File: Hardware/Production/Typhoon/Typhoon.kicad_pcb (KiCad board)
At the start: 4 copper layers, 16 parts, among them U3 LM66200DRLR, U4 MAX77827AEFD+T, U5 SC4215ASTRT

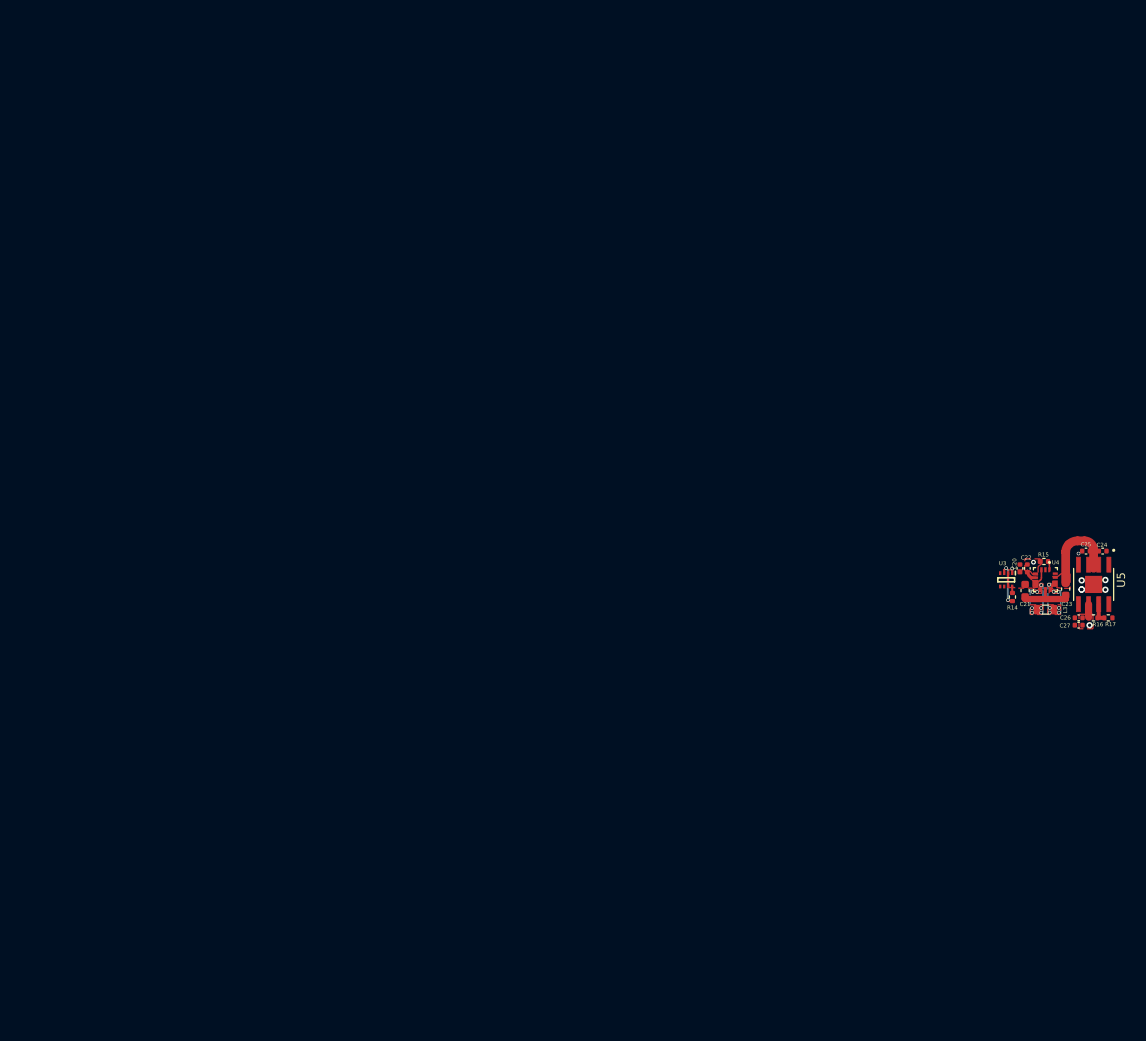
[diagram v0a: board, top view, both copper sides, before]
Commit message: Finished footprinting and started the PCB layout
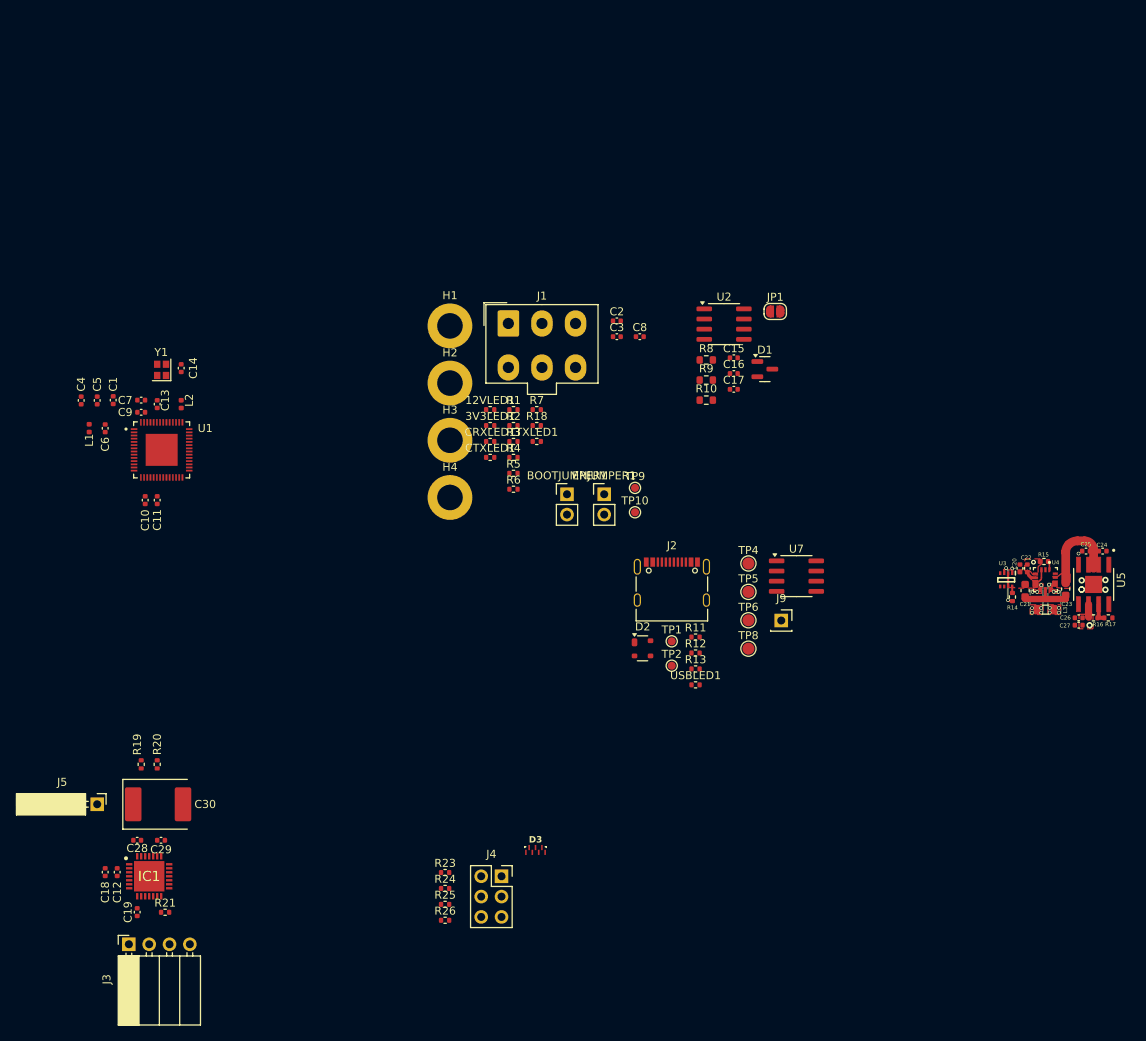
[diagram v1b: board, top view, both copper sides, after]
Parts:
- added 12VLED1: RED_LED, Resistor_SMD:R_0402_1005Metric, F.Cu at (103.5, 65.8)
- added 3V3LED1: BLUE_LED, Resistor_SMD:R_0402_1005Metric, F.Cu at (103.5, 67.8)
- added BOOTJUMPER1: Conn_01x02_Male, Connector_PinHeader_2.54mm:PinHeader_1x02_P2.54mm_Vertical, F.Cu at (113.2, 76.3)
- added C1: 10uF, Capacitor_SMD:C_0402_1005Metric, F.Cu at (56.4, 64.6)
- added C10: 0.1uF, Capacitor_SMD:C_0402_1005Metric, F.Cu at (60.4, 77.1)
- added C11: 0.1uF, Capacitor_SMD:C_0402_1005Metric, F.Cu at (61.9, 77.1)
- added C12: 22n, Capacitor_SMD:C_0402_1005Metric, F.Cu at (56.9, 123.6)
- added C13: 11pF, Capacitor_SMD:C_0402_1005Metric, F.Cu at (61.9, 65.1)
- added C14: 11pF, Capacitor_SMD:C_0402_1005Metric, F.Cu at (64.9, 60.6)
- added C15: 100nF, Capacitor_SMD:C_0402_1005Metric, F.Cu at (134.0, 59.3)
- added C16: 10uF, Capacitor_SMD:C_0402_1005Metric, F.Cu at (134.0, 61.2)
- added C17: 47nF, Capacitor_SMD:C_0402_1005Metric, F.Cu at (134.0, 63.2)
- added C18: 100n, Capacitor_SMD:C_0402_1005Metric, F.Cu at (55.4, 123.6)
- added C19: 2.2u, Capacitor_SMD:C_0402_1005Metric, F.Cu at (59.4, 128.6)
- added C2: 1uF, Capacitor_SMD:C_0402_1005Metric, F.Cu at (119.4, 54.7)
- added C28: 100n, Capacitor_SMD:C_0402_1005Metric, F.Cu at (59.4, 119.6)
- added C29: 100n, Capacitor_SMD:C_0402_1005Metric, F.Cu at (62.4, 119.6)
- added C3: 0.1uF, Capacitor_SMD:C_0402_1005Metric, F.Cu at (119.4, 56.6)
- added C30: 100u, Capacitor_Tantalum_SMD:CP_EIA-7360-38_Kemet-E, F.Cu at (62.0, 115.1)
- added C4: 1uF, Capacitor_SMD:C_0402_1005Metric, F.Cu at (52.4, 64.6)
- added C5: 0.1uF, Capacitor_SMD:C_0402_1005Metric, F.Cu at (54.4, 64.6)
- added C6: 0.1uF, Capacitor_SMD:C_0402_1005Metric, F.Cu at (55.4, 68.1)
- added C7: 1uF, Capacitor_SMD:C_0402_1005Metric, F.Cu at (59.9, 64.6)
- added C8: 0.1uF, Capacitor_SMD:C_0402_1005Metric, F.Cu at (122.2, 56.6)
- added C9: 10nF, Capacitor_SMD:C_0402_1005Metric, F.Cu at (59.9, 66.1)
- added CRXLED1: ORANGE_LED, Resistor_SMD:R_0402_1005Metric, F.Cu at (103.5, 69.7)
- added CTXLED1: GREEN_LED, Resistor_SMD:R_0402_1005Metric, F.Cu at (103.5, 71.7)
- added D1: SM712_SOT23, Package_TO_SOT_SMD:SOT-23, F.Cu at (137.9, 60.7)
- added D2: SP0503BAHT, Package_TO_SOT_SMD:SOT-143, F.Cu at (122.6, 95.6)
- added D3: RCLAMP3346PQTNT, iclr:RCLAMP3346PQTNT, F.Cu at (109.2, 120.8)
- added ENJUMPER1: Conn_01x02_Male, Connector_PinHeader_2.54mm:PinHeader_1x02_P2.54mm_Vertical, F.Cu at (117.8, 76.3)
- added H1: MountingHole_Pad, MountingHole:MountingHole_3.2mm_M3_DIN965_Pad, F.Cu at (98.5, 55.3)
- added H2: MountingHole_Pad, MountingHole:MountingHole_3.2mm_M3_DIN965_Pad, F.Cu at (98.5, 62.4)
- added H3: MountingHole_Pad, MountingHole:MountingHole_3.2mm_M3_DIN965_Pad, F.Cu at (98.5, 69.6)
- added H4: MountingHole_Pad, MountingHole:MountingHole_3.2mm_M3_DIN965_Pad, F.Cu at (98.5, 76.7)
- added IC1: TMC2209-LA, iclr:QFN50P500X500X90-29N, F.Cu at (60.9, 124.1)
- added J1: RBUS, Connector_Molex:Molex_Mini-Fit_Jr_5566-06A_2x03_P4.20mm_Vertical, F.Cu at (105.8, 55.0)
- added J2: USB_C_Receptacle_USB2.0, Connector_USB:USB_C_Receptacle_Palconn_UTC16-G, F.Cu at (126.3, 87.3)
- added J3: Motor Breakout, Connector_PinSocket_2.54mm:PinSocket_1x04_P2.54mm_Horizontal, F.Cu at (58.4, 132.6)
- added J4: GPIO Breakout, Connector_PinSocket_2.54mm:PinSocket_2x03_P2.54mm_Vertical, F.Cu at (105.0, 124.1)
- added J5: Power in, Connector_PinSocket_2.54mm:PinSocket_1x01_P2.54mm_Horizontal, F.Cu at (54.4, 115.1)
- added J9: Conn_01x01_Socket, Connector_PinSocket_2.54mm:PinSocket_1x01_P2.54mm_Vertical, F.Cu at (139.9, 92.1)
- added JP1: TermJP, Jumper:SolderJumper-2_P1.3mm_Open_RoundedPad1.0x1.5mm, F.Cu at (139.2, 53.5)
- added L1: 2.0nH, Inductor_SMD:L_0402_1005Metric, F.Cu at (53.4, 68.1)
- added L2: 20nH, Inductor_SMD:L_0402_1005Metric, F.Cu at (64.9, 65.1)
- added R1: 10K, Resistor_SMD:R_0402_1005Metric, F.Cu at (106.5, 65.8)
- added R10: 60, Resistor_SMD:R_0603_1608Metric, F.Cu at (130.6, 64.6)
- added R11: 5.1k, Resistor_SMD:R_0402_1005Metric, F.Cu at (129.2, 94.2)
- added R12: 5.1k, Resistor_SMD:R_0402_1005Metric, F.Cu at (129.2, 96.2)
- added R13: 5.1k, Resistor_SMD:R_0402_1005Metric, F.Cu at (129.2, 98.2)
- added R18: 1k, Resistor_SMD:R_0402_1005Metric, F.Cu at (109.4, 67.8)
- added R19: 0.1, Resistor_SMD:R_0402_1005Metric, F.Cu at (59.9, 110.1)
- added R2: 470, Resistor_SMD:R_0402_1005Metric, F.Cu at (106.5, 67.8)
- added R20: 0.1, Resistor_SMD:R_0402_1005Metric, F.Cu at (61.9, 110.1)
- added R21: 1k, Resistor_SMD:R_0402_1005Metric, F.Cu at (62.9, 128.6)
- added R23: 10k, Resistor_SMD:R_0402_1005Metric, F.Cu at (97.9, 123.6)
- added R24: 10k, Resistor_SMD:R_0402_1005Metric, F.Cu at (97.9, 125.6)
- added R25: 10k, Resistor_SMD:R_0402_1005Metric, F.Cu at (97.9, 127.6)
- added R26: 10k, Resistor_SMD:R_0402_1005Metric, F.Cu at (97.9, 129.6)
- added R3: 10K, Resistor_SMD:R_0402_1005Metric, F.Cu at (106.5, 69.7)
- added R4: 470, Resistor_SMD:R_0402_1005Metric, F.Cu at (106.5, 71.7)
- added R5: 1k, Resistor_SMD:R_0402_1005Metric, F.Cu at (106.5, 73.7)
- added R6: 499R, Resistor_SMD:R_0402_1005Metric, F.Cu at (106.5, 75.7)
- added R7: 3k, Resistor_SMD:R_0402_1005Metric, F.Cu at (109.4, 65.8)
- added R8: 0, Resistor_SMD:R_0603_1608Metric, F.Cu at (130.6, 59.5)
- added R9: 60, Resistor_SMD:R_0603_1608Metric, F.Cu at (130.6, 62.1)
- added TP1: TestPoint, TestPoint:TestPoint_Pad_D1.0mm, F.Cu at (126.2, 94.7)
- added TP10: TestPoint, TestPoint:TestPoint_Pad_D1.0mm, F.Cu at (121.7, 78.6)
- added TP2: TestPoint, TestPoint:TestPoint_Pad_D1.0mm, F.Cu at (126.2, 97.8)
- added TP4: TestPoint, TestPoint:TestPoint_Pad_D1.5mm, F.Cu at (135.8, 85.0)
- added TP5: TestPoint, TestPoint:TestPoint_Pad_D1.5mm, F.Cu at (135.8, 88.5)
- added TP6: TestPoint, TestPoint:TestPoint_Pad_D1.5mm, F.Cu at (135.8, 92.1)
- added TP8: TestPoint, TestPoint:TestPoint_Pad_D1.5mm, F.Cu at (135.8, 95.6)
- added TP9: TestPoint, TestPoint:TestPoint_Pad_D1.0mm, F.Cu at (121.7, 75.5)
- added TXLED1: GREEN_LED, Resistor_SMD:R_0402_1005Metric, F.Cu at (109.4, 69.7)
- added U1: ESP32-S3, iclr:QFN40P700X700X90-57N, F.Cu at (62.5, 70.8)
- added U2: SN65HVD230, Package_SO:SOIC-8_3.9x4.9mm_P1.27mm, F.Cu at (132.8, 55.1)
- added U7: XL1509-3.3, Package_SO:SOIC-8_3.9x4.9mm_P1.27mm, F.Cu at (141.8, 86.6)
- added USBLED1: WHITE_LED, Resistor_SMD:R_0402_1005Metric, F.Cu at (129.2, 100.2)
- added Y1: R940000171, Crystal:Crystal_SMD_2016-4Pin_2.0x1.6mm, F.Cu at (62.5, 60.8)

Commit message: Slight updates to the schematic and more PCB layout
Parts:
- removed J5: Power in, Connector_PinSocket_2.54mm:PinSocket_1x01_P2.54mm_Horizontal
- moved R9 46.3 mm to (158.9, 25.4), turned to -90 degrees
- moved R10 45.4 mm to (158.9, 29.1), turned to 90 degrees
- moved R8 44.3 mm to (147.4, 18.6), turned to 180 degrees
- moved D1 39.0 mm to (154.9, 25.6), turned to 180 degrees
- moved C17 37.5 mm to (139.4, 26.1), turned to 90 degrees
- moved C16 35.9 mm to (141.4, 26.1), turned to 90 degrees
- moved C15 34.4 mm to (142.9, 26.1), turned to 90 degrees
- moved U2 32.5 mm to (147.4, 26.1)
- moved JP1 28.9 mm to (155.4, 29.6)
- moved R25 14.6 mm to (112.4, 129.1), turned to 90 degrees
- moved R23 10.5 mm to (103.4, 132.6)
- moved D3 6.32 mm to (108.6, 127.1), turned to -90 degrees
- moved R26 3.59 mm to (95.9, 126.6), turned to 90 degrees
- moved R24 1.41 mm to (98.9, 126.6), turned to 90 degrees
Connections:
- C18 pad 1: /Stepper_Driver/VSS -> +16.8V
- C28 pad 1: /Stepper_Driver/VSS -> +16.8V
- C29 pad 2: /Stepper_Driver/VSS -> +16.8V
- C30 pad 1: /Stepper_Driver/VSS -> +16.8V
- IC1 pad 22: /Stepper_Driver/VSS -> +16.8V
- IC1 pad 28: /Stepper_Driver/VSS -> +16.8V

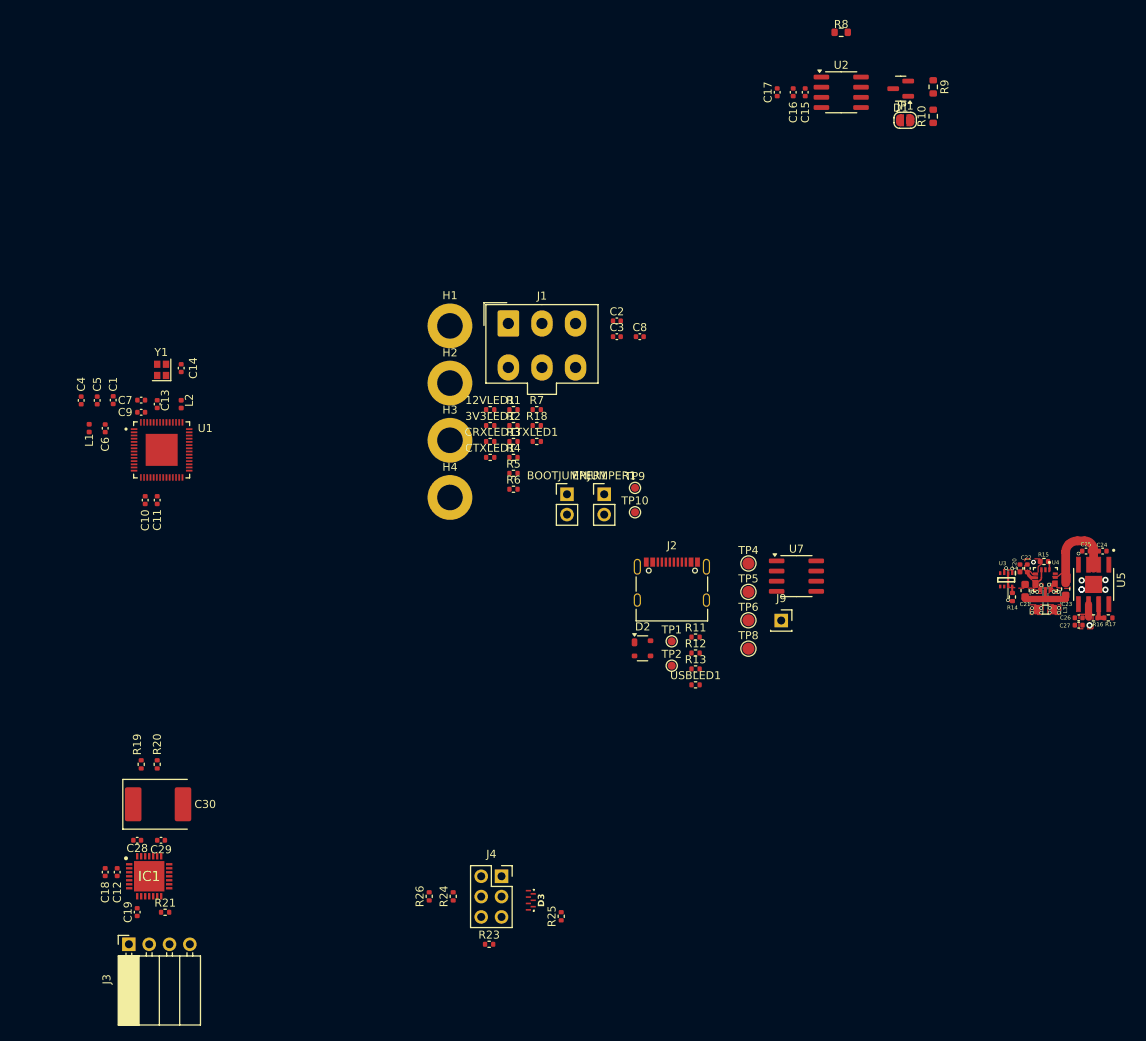
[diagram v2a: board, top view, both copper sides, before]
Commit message: Rough Board Layout (Need Review)
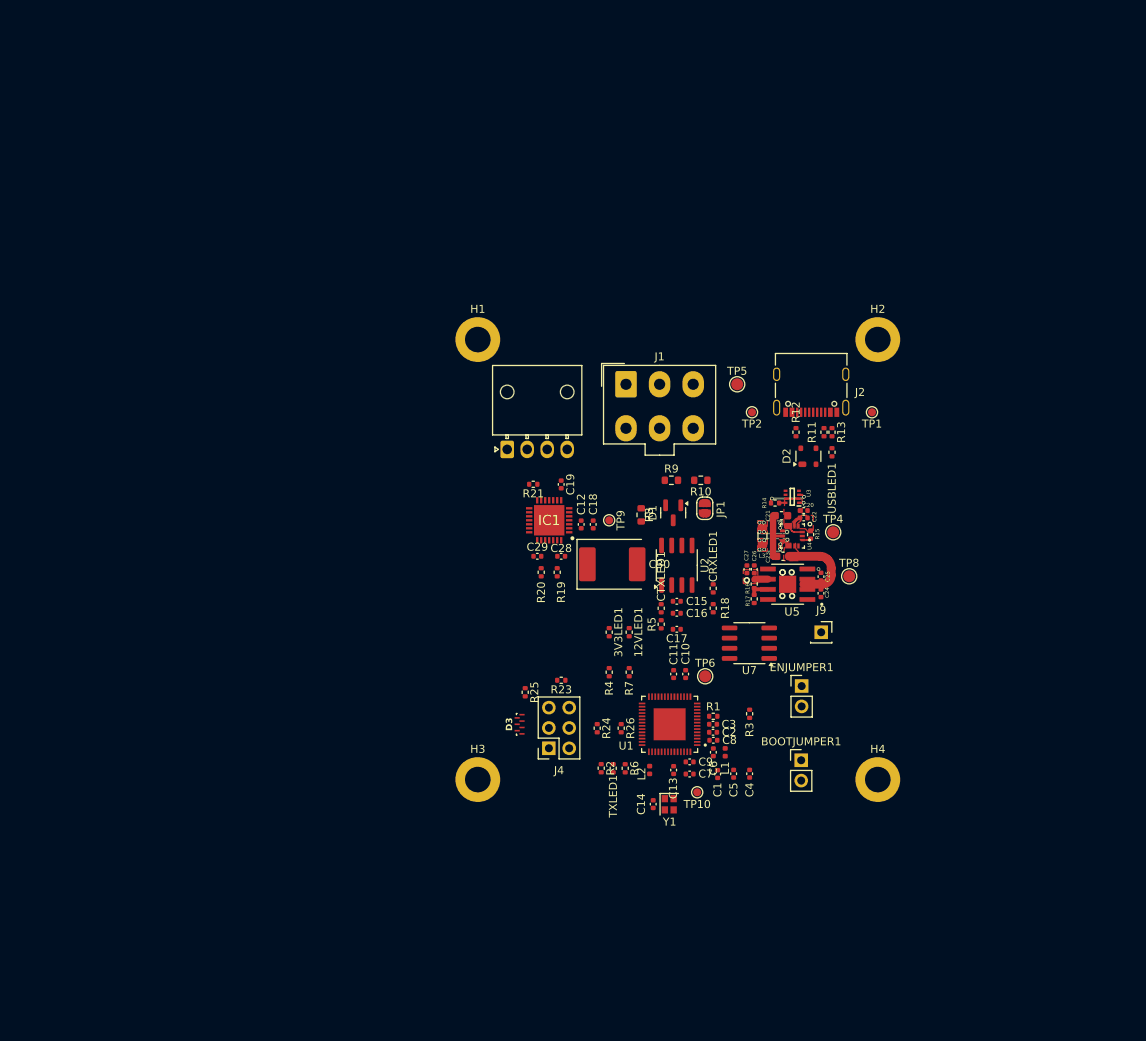
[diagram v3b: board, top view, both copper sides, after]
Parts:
- J3: footprint Connector_PinSocket_2.54mm:PinSocket_1x04_P2.54mm_Horizontal -> iclr:Molex_Nano-Fit_105313-xx04_1x04_P2.50mm_Horizontal
- moved C4 95.7 mm to (136.0, 111.3), turned to -90 degrees
- moved C5 92.2 mm to (134.0, 111.3), turned to -90 degrees
- moved L1 89.2 mm to (132.9, 108.6), turned to 90 degrees
- moved C1 88.8 mm to (132.0, 111.3), turned to -90 degrees
- moved C6 86.1 mm to (131.4, 108.6), turned to -90 degrees
- moved Y1 83.5 mm to (125.9, 115.1), turned to -90 degrees
- moved C7 83.0 mm to (128.5, 111.3), turned to 0 degrees
- moved C9 81.3 mm to (128.5, 109.8), turned to 0 degrees
- moved C14 80.3 mm to (123.9, 115.1), turned to -90 degrees
- moved C13 79.1 mm to (126.5, 110.8), turned to -90 degrees
- moved J3 77.9 mm to (105.7, 70.7)
- moved C19 75.3 mm to (112.4, 75.1), turned to -90 degrees
- moved C18 74.9 mm to (116.4, 80.1), turned to 90 degrees
- moved L2 74.3 mm to (123.5, 110.8), turned to -90 degrees
- moved C12 72.5 mm to (114.9, 80.1), turned to 90 degrees
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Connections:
- J3 pad 1: /Stepper_Driver/OB2 -> /Stepper_Driver/OA2
- J3 pad 2: /Stepper_Driver/OB1 -> /Stepper_Driver/OA1
- J3 pad 3: /Stepper_Driver/OA1 -> /Stepper_Driver/OB1
- J3 pad 4: /Stepper_Driver/OA2 -> /Stepper_Driver/OB2
